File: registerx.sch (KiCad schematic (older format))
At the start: 8 parts, among them U32 74LS245, U33 74LS173, U34 74LS173, U35 74LS245, U36 74LS173, U37 74LS173

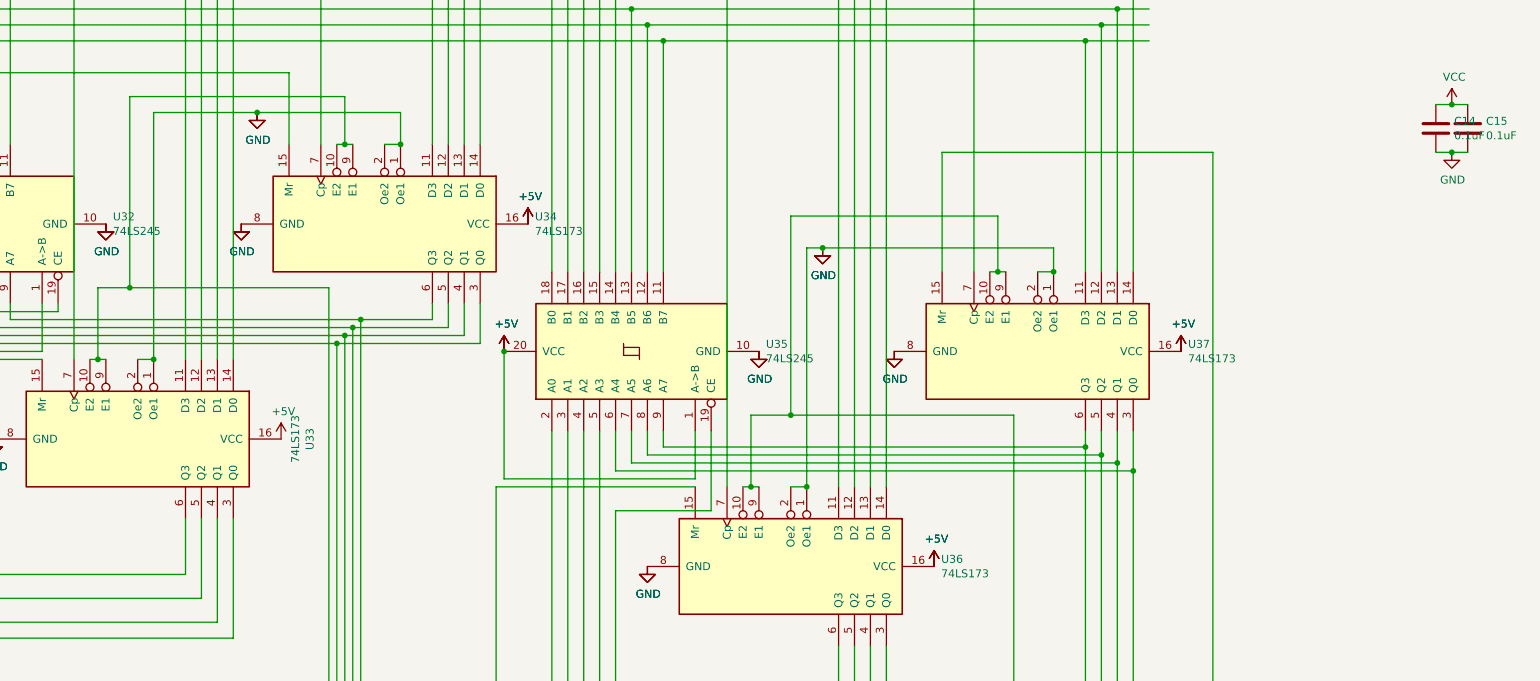
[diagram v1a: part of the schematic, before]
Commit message: added display
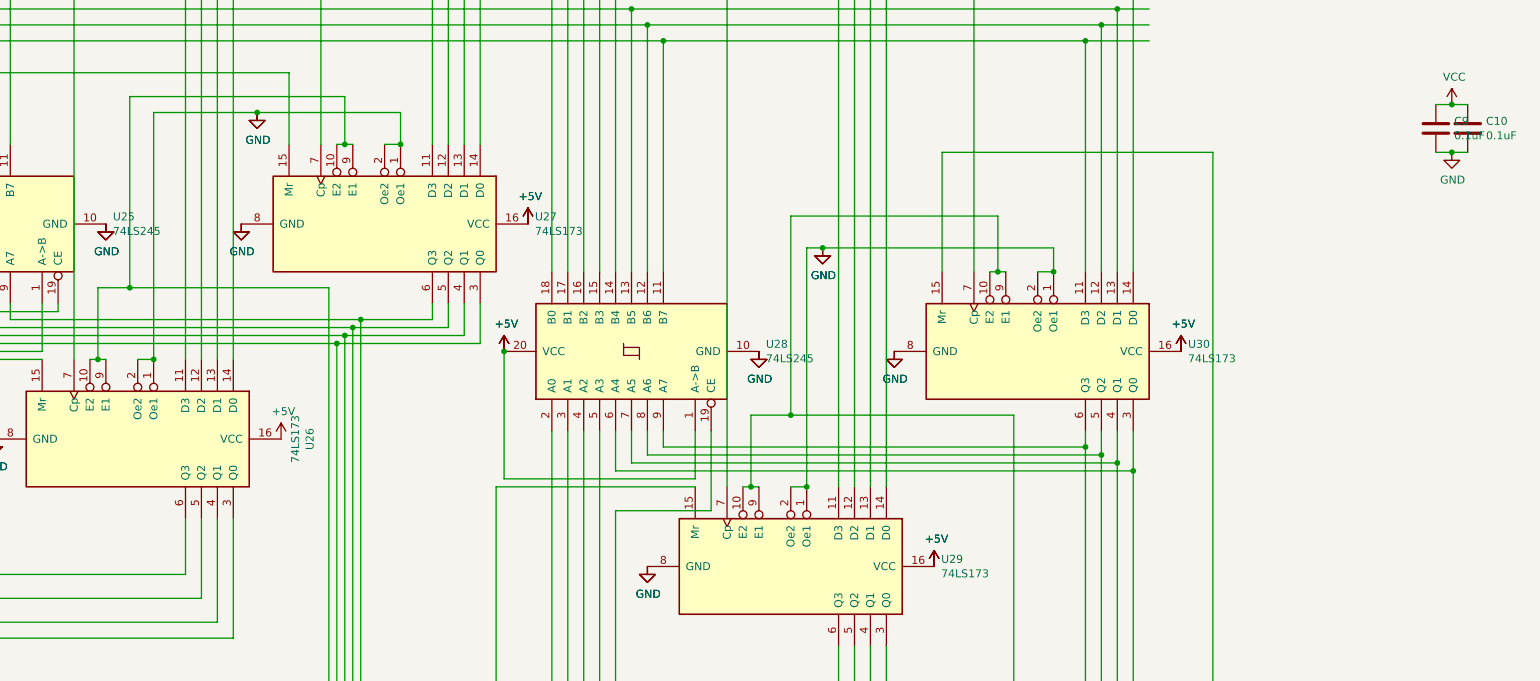
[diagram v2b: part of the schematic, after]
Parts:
- renumbered C15 to C10, C14 to C9, U32 to U25, U33 to U26, U34 to U27, U35 to U28, U36 to U29, U37 to U30

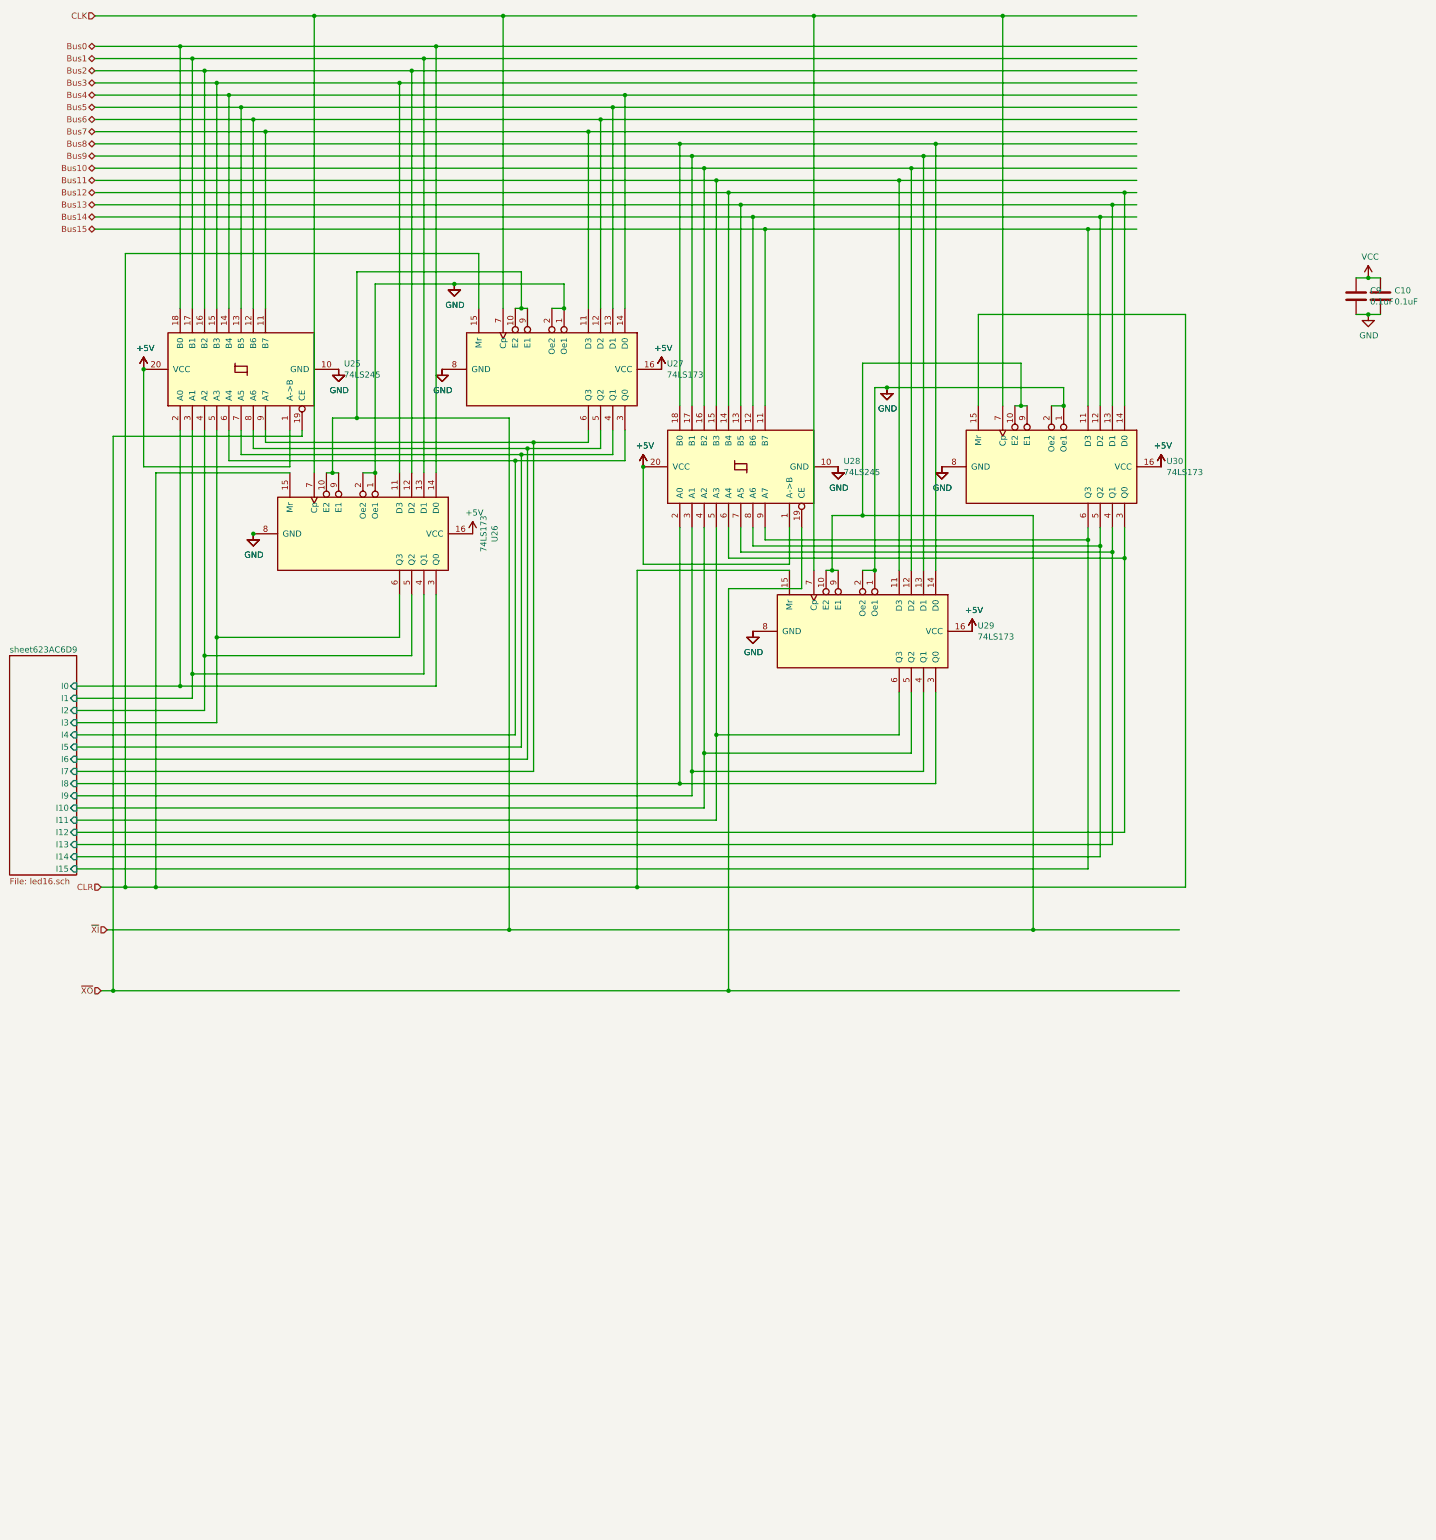
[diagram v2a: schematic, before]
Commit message: added swp_x, and cleanup readme
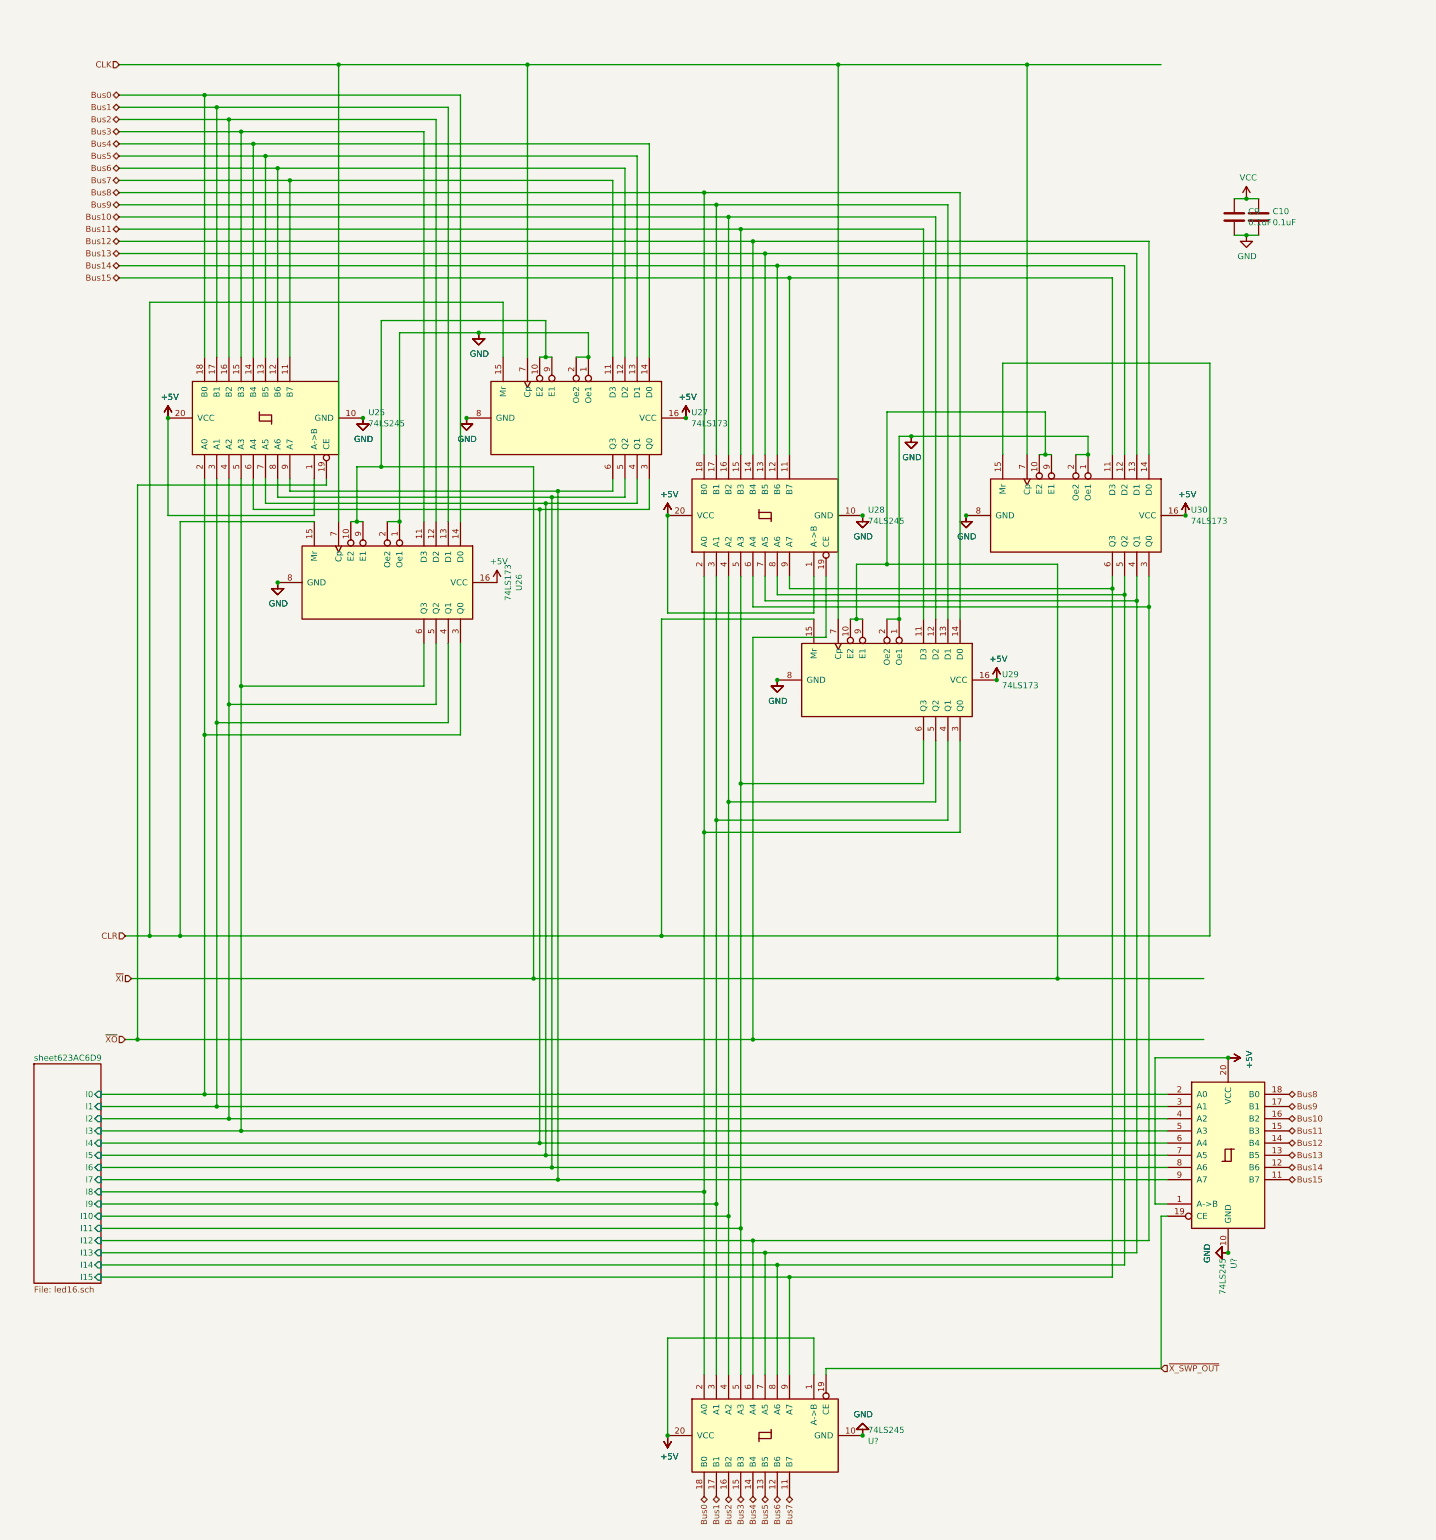
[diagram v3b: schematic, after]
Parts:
- added U? (x2): 74LS245, Package_DIP:DIP-20_W7.62mm, symbol 16bitCpu-rescue:74LS245-74xx
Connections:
- net labels added: ~X_SWP_OUT
- wire segments 241 -> 257
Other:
- moved on the sheet: C10, C9, U25, U26, U27, U28, U29, U30

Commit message: clean up
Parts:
- gave numbers to parts that had none: 2
- renumbered U29 to U30, U30 to U31
